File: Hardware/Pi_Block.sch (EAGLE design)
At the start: 46 parts, among them U1 PCA9306, U2 EDISON_CONNECTOR_FULLMOUNTING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, U3 EDISON_CONNECTOR_FULLHEADER, U4 TPS62065, U5 MIC5219 3.3V

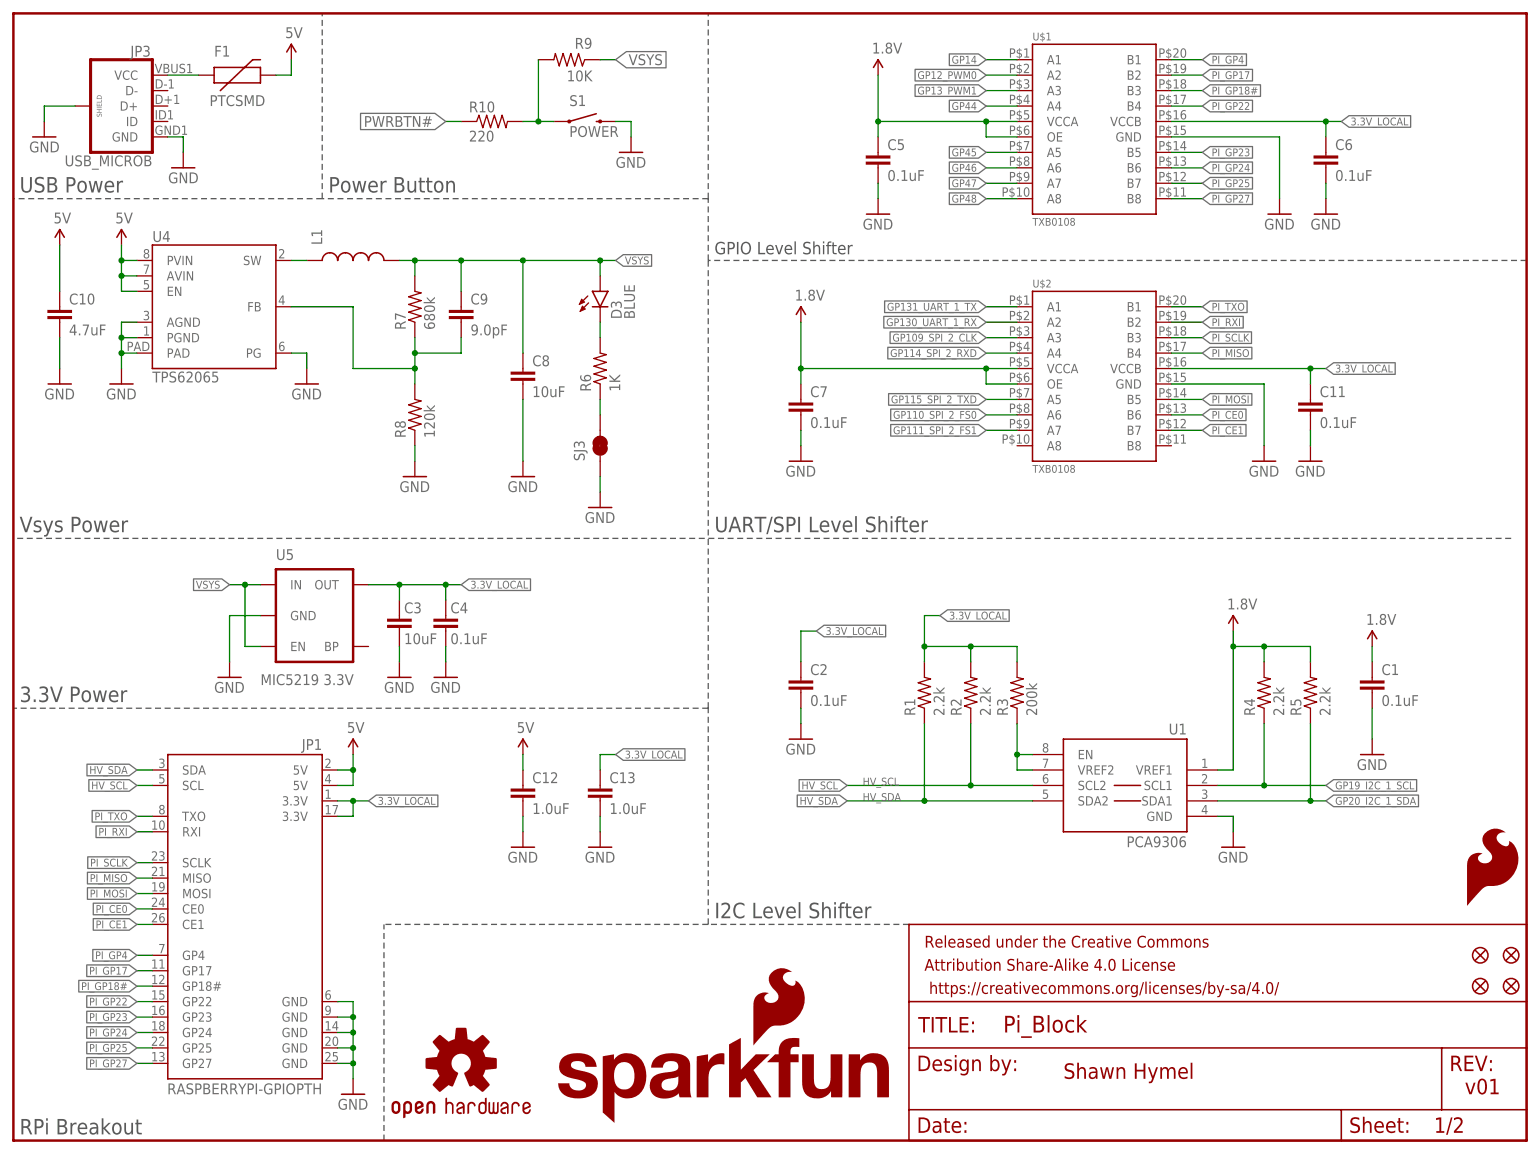
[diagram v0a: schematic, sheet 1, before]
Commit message: Replaced Header footprint Included DCIN pin Renamed boards Renamed files Replaces power button with side shooting SMD Cleaned up dimensions
TODO: solve power situation between VSYS and DCIN
TODO: Add pass through via for DCIN
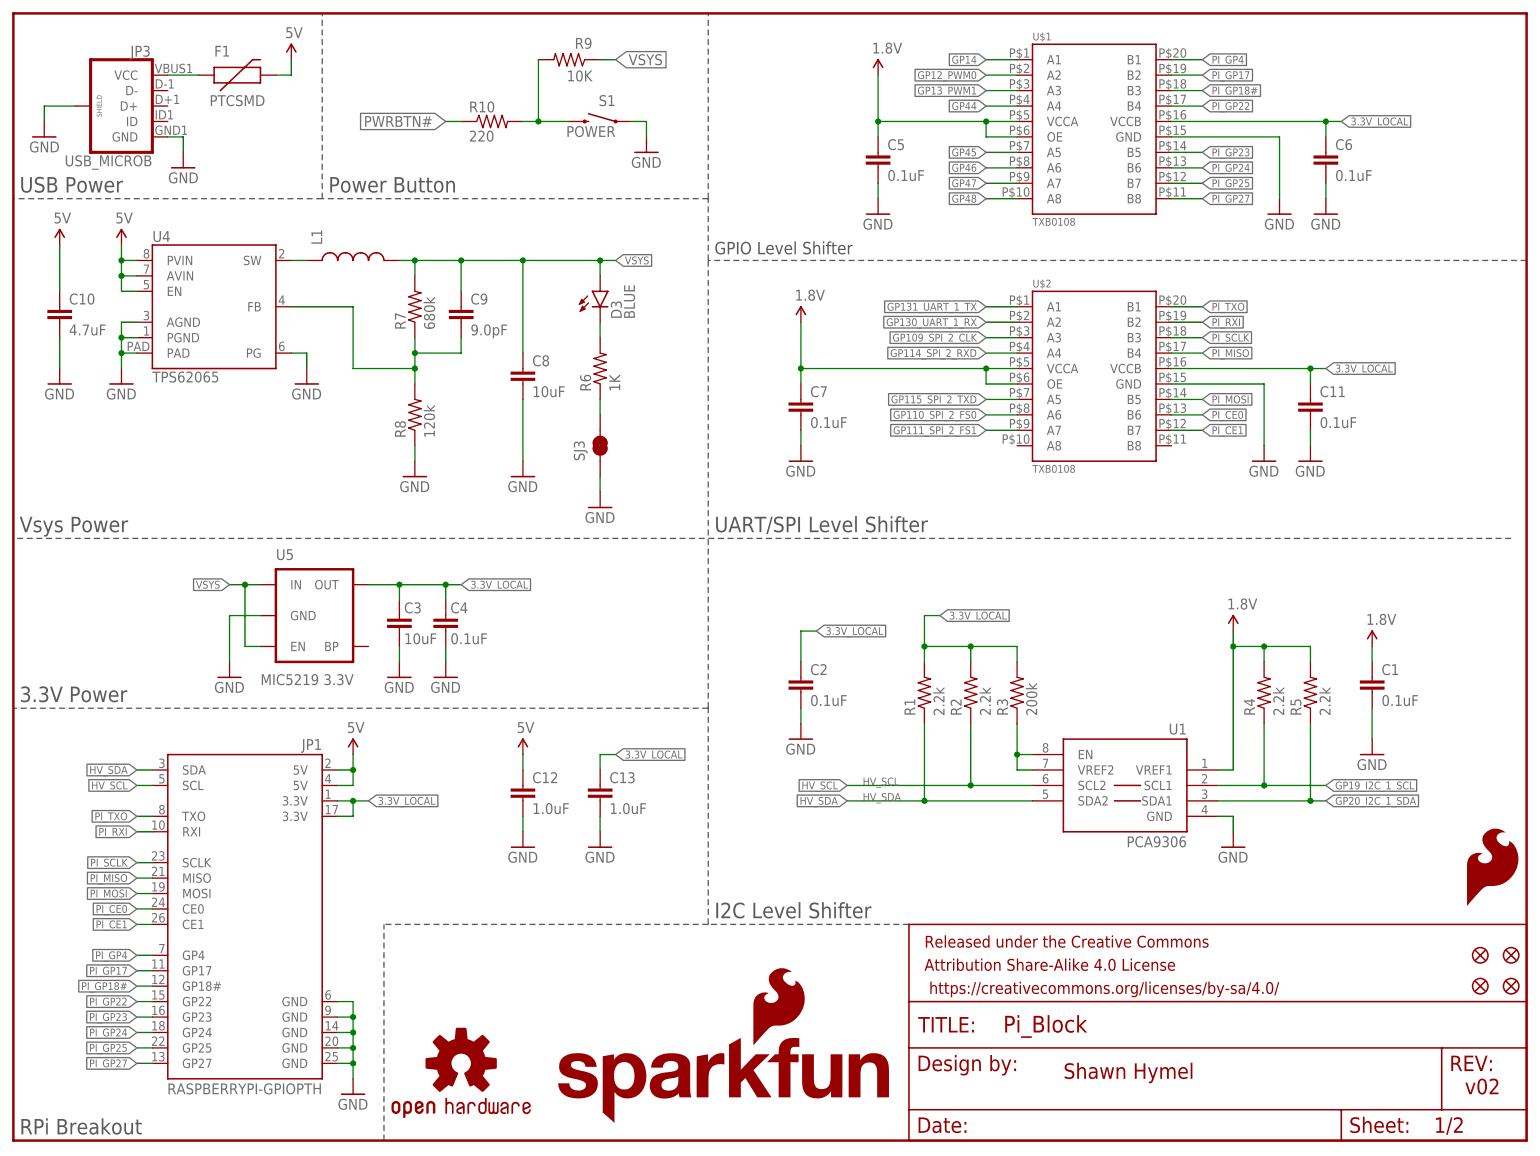
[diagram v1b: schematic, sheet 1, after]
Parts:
- S1: device SparkFun-Electromechanical:SWITCH-MOMENTARY-2-SMD-1101NE -> SparkFun-Electromechanical:SWITCH-MOMENTARY-2TACTILE-SWITCH-SMD-RIGHT-ANGLE
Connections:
- new net DCIN: U2.DCIN, U3.DCIN
- net GND: now also S1.1; no longer S1.2
- net N$15: now also S1.2; no longer S1.1
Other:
- note added: "v02"
- note removed: "v01"
- moved on the sheet: S1
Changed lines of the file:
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@@
 <part name="GND24" library="SparkFun-Aesthetics" deviceset="GND" device=""/>
 <part name="GND25" library="SparkFun-Aesthetics" deviceset="GND" device=""/>
-<part name="S1" library="SparkFun-Electromechanical" deviceset="SWITCH-MOMENTARY-2" device="-SMD-1101NE" value="POWER"/>
+<part name="S1" library="SparkFun-Electromechanical" deviceset="SWITCH-MOMENTARY-2" device="TACTILE-SWITCH-SMD-RIGHT-ANGLE" value="POWER"/>
 <part name="R9" library="SparkFun-Resistors" deviceset="10KOHM1/10W1%(0603)" device="0603" value="10K"/>
 <part name="R10" library="SparkFun-Resistors" deviceset="RESISTOR" device="0603" value="220">
@@
 <sheet>
 <plain>
-<text x="238.76" y="7.62" size="2.54" layer="94">v01</text>
+<text x="238.76" y="7.62" size="2.54" layer="94">v02</text>
 <text x="172.72" y="10.16" size="2.54" layer="94">Shawn Hymel</text>
 <wire x1="114.3" y1="35.56" x2="114.3" y2="71.12" width="0.1524" layer="97" style="longdash"/>
@@
 <instance part="GND24" gate="1" x="83.82" y="48.26"/>
 <instance part="GND25" gate="1" x="96.52" y="48.26"/>
-<instance part="S1" gate="G$1" x="93.98" y="167.64"/>
+<instance part="S1" gate="G$1" x="96.52" y="167.64" rot="MR0"/>
 <instance part="R9" gate="G$1" x="91.44" y="177.8" smashed="yes" rot="R180">
 <attribute name="NAME" x="95.25" y="181.3814" size="1.778" layer="95" rot="R180"/>
@@
 <attribute name="PROD_ID" x="78.74" y="167.64" size="1.778" layer="96" display="off"/>
 </instance>
-<instance part="GND26" gate="1" x="101.6" y="162.56"/>
+<instance part="GND26" gate="1" x="104.14" y="162.56"/>
 <instance part="LOGO3" gate="G$1" x="238.76" y="38.1"/>
 </instances>
@@
 </segment>
 <segment>
-<pinref part="S1" gate="G$1" pin="2"/>
-<wire x1="99.06" y1="167.64" x2="101.6" y2="167.64" width="0.1524" layer="91"/>
-<wire x1="101.6" y1="167.64" x2="101.6" y2="165.1" width="0.1524" layer="91"/>
+<wire x1="104.14" y1="167.64" x2="104.14" y2="165.1" width="0.1524" layer="91"/>
 <pinref part="GND26" gate="1" pin="GND"/>
+<pinref part="S1" gate="G$1" pin="1"/>
+<wire x1="101.6" y1="167.64" x2="104.14" y2="167.64" width="0.1524" layer="91"/>
 </segment>
 <segment>
@@
 <wire x1="83.82" y1="167.64" x2="86.36" y2="167.64" width="0.1524" layer="91"/>
 <wire x1="86.36" y1="167.64" x2="86.36" y2="177.8" width="0.1524" layer="91"/>
-<pinref part="S1" gate="G$1" pin="1"/>
-<wire x1="86.36" y1="167.64" x2="88.9" y2="167.64" width="0.1524" layer="91"/>
 <junction x="86.36" y="167.64"/>
+<pinref part="S1" gate="G$1" pin="2"/>
+<wire x1="86.36" y1="167.64" x2="91.44" y2="167.64" width="0.1524" layer="91"/>
 </segment>
 </net>
@@
 </segment>
 </net>
+<net name="DCIN" class="0">
+<segment>
+<pinref part="U3" gate="G$1" pin="DCIN"/>
+<wire x1="172.72" y1="152.4" x2="170.18" y2="152.4" width="0.1524" layer="91"/>
+<label x="170.18" y="152.4" size="1.27" layer="95" rot="R180" xref="yes"/>
+</segment>
+<segment>
+<pinref part="U2" gate="G$1" pin="DCIN"/>
+<wire x1="25.4" y1="152.4" x2="22.86" y2="152.4" width="0.1524" layer="91"/>
+<label x="22.86" y="152.4" size="1.27" layer="95" rot="R180" xref="yes"/>
+</segment>
+</net>

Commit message: Added Vsys-to-5V diode. Added DCIN to Vsys MOSFET. Added slants to board dimension near Pi connector for stability.
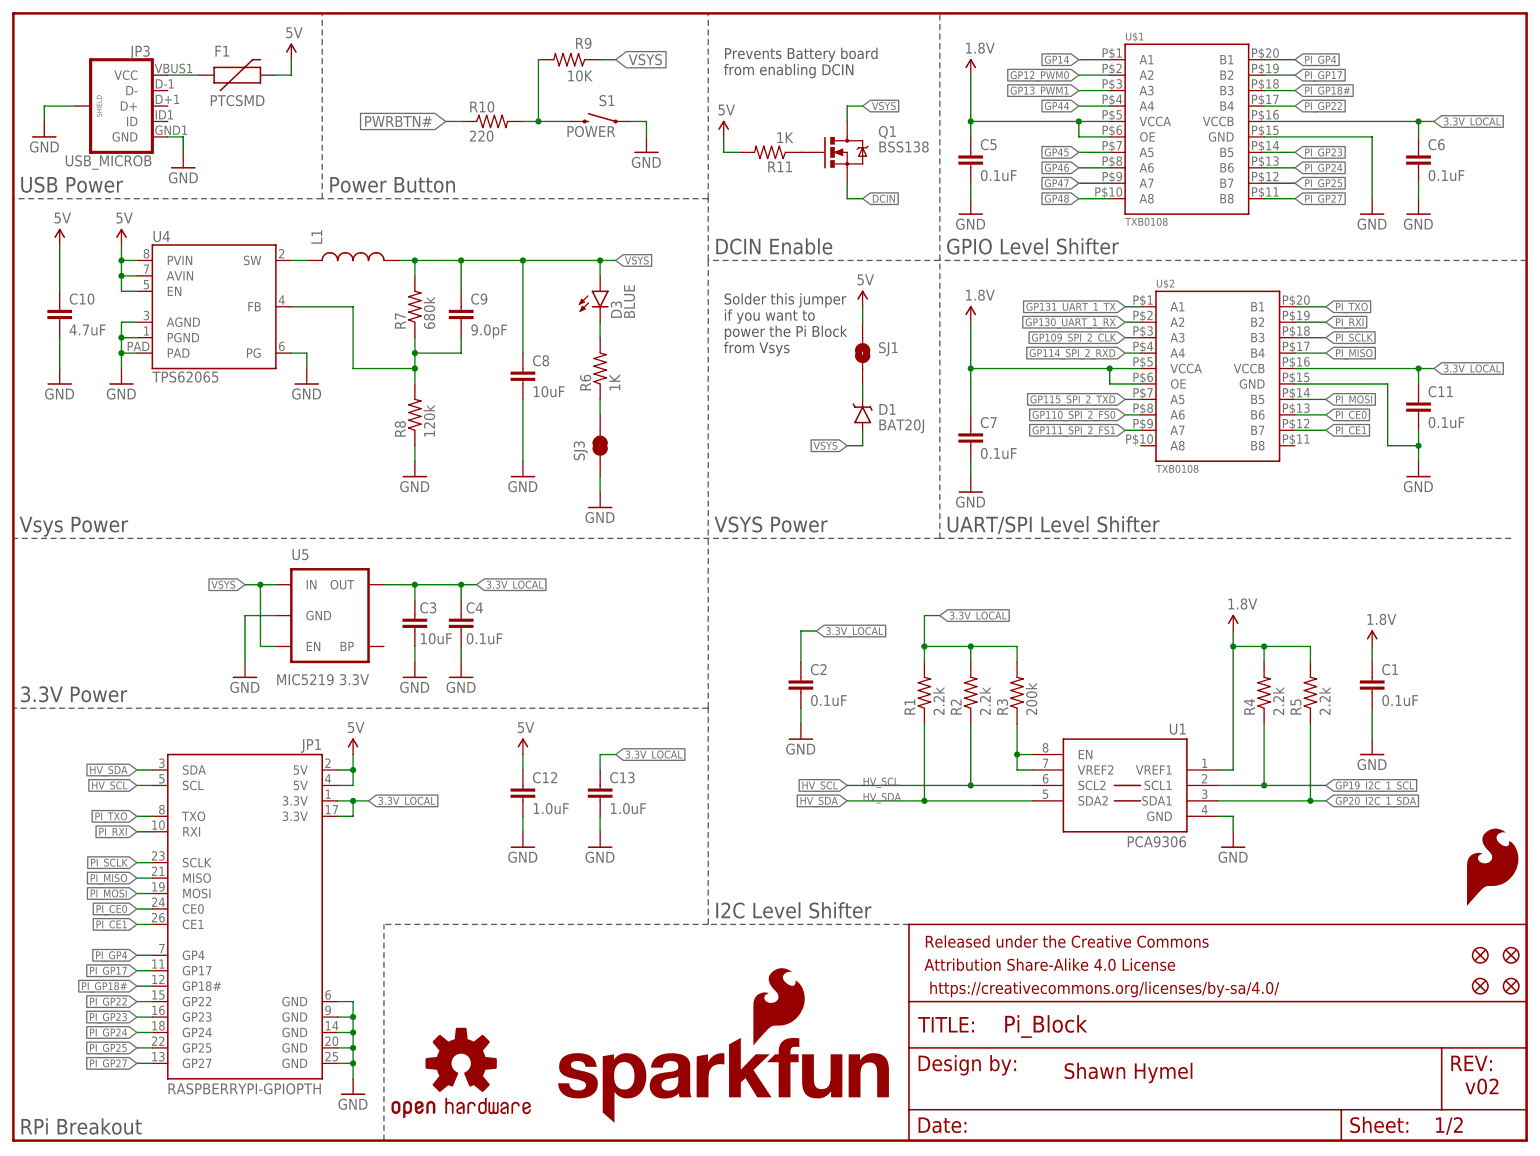
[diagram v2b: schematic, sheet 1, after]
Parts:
- added D1: BAT20J, SparkFun-DiscreteSemi:DIODE-SCHOTTKY-BAT20J
- added Q1: BSS138, SparkFun-DiscreteSemi:MOSFET-NCHANNELBSS138
- added R11: 1K, SparkFun-Resistors:1KOHM1/10W1%(0603)
- added SJ1: JUMPER-PAD-2-NOYES_SILK, SparkFun-Passives:JUMPER-PAD-2-NOYES_SILK
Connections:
- new net N$16: Q1.G, R11.1
- new net N$3: D1.C, SJ1.2
- net 5V: now also R11.2, SJ1.1
- net DCIN: now also Q1.S
- net VSYS: now also D1.A, Q1.D
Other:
- note added: "DCIN Enable"
- note added: "Prevents Battery board from enabling DCIN"
- note added: "Solder this jumper if you want to power the Pi Block from Vsys"
- note added: "VSYS Power"
- moved on the sheet: C11, C3, C4, C5, C6, C7, U$1, U$2, U5
